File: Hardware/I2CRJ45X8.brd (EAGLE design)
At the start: 80 x 50 mm, 56 parts, among them IC1 MCP23017SO, IC2 MCP23017SO, J1 I2C-BREAKOUT, J2 INT2A, J3 M02X3-PIN, J4 M02X3-PIN, J5 RJ45-X8, J6 I2C-BREAKOUT, J7 INT1A

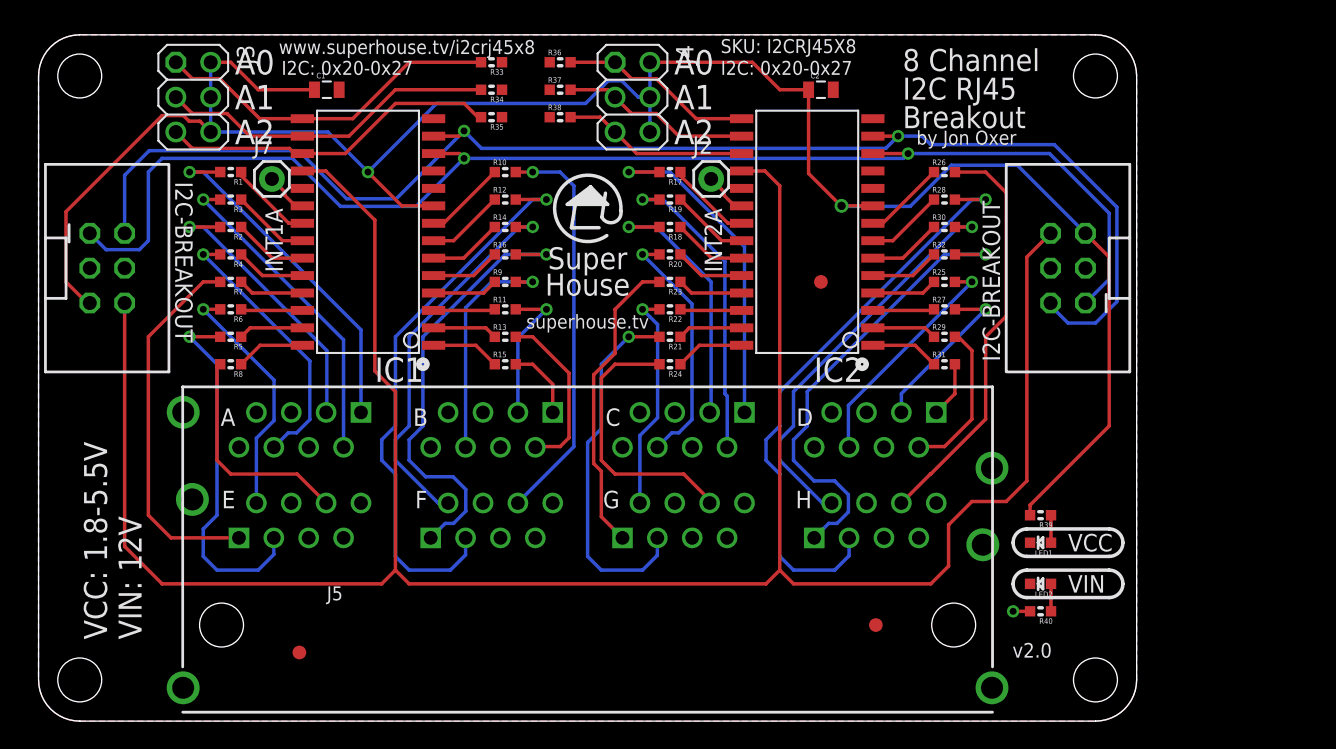
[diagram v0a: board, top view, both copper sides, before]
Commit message: Reduced width of PCB. Adjusted mounting hole locations. Improved GND connections. Changed position of power LEDs.
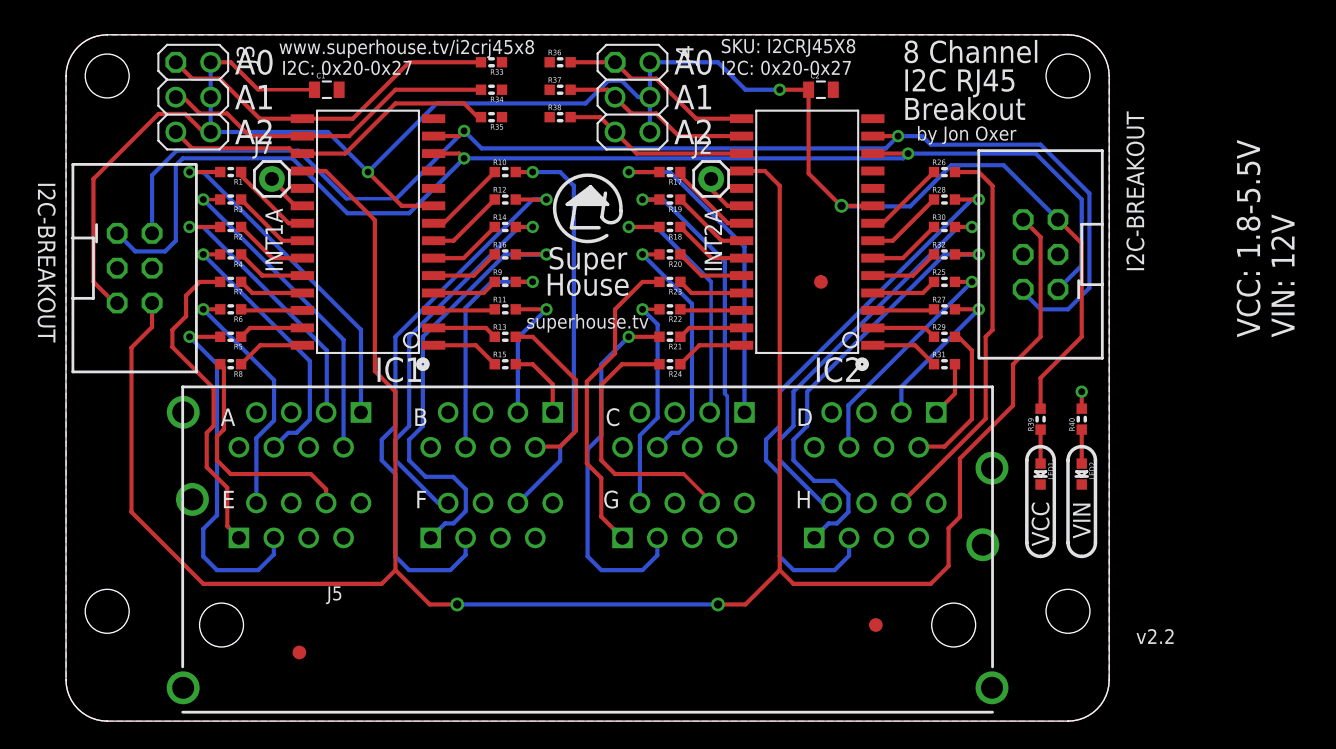
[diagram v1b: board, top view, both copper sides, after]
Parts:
- moved R40 14.3 mm to (76.0, 22.0), turned to 90 degrees
- moved LED2 8.54 mm to (76.0, 18.0), turned to 270 degrees
- moved R39 7.00 mm to (73.0, 22.0), turned to 90 degrees
- moved LED1 5.00 mm to (73.0, 18.0), turned to 270 degrees
- moved J1 2.24 mm to (73.0, 34.0)
- moved J6 2.00 mm to (7.00, 33.0)
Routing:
- net VCC: track 151.1 -> 140.3 mm, vias 2 -> 3
- net SDA: track 101.1 -> 96.7 mm
- net E1: track 27.2 -> 23.4 mm
- net SCL: track 97.5 -> 93.9 mm
- net H6: track 30.2 -> 29.0 mm
- net H3: track 43.1 -> 42.1 mm
- net H1: track 34.4 -> 33.4 mm
- net E6: track 16.3 -> 17.1 mm
- net D3: track 12.3 -> 11.6 mm
- net !RESET: track 174.0 -> 173.6 mm, vias 0 -> 2
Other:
- board size 80 x 50 mm -> 76 x 50 mm
- board text added: "(C)2019-2021 SuperHouse Automation Pty Ltd Released under the terms of the TAPR Open Hardware License: www.tapr.org/OHL"
- board text added: "v2.2"
- board text removed: "(C)2019-2020 SuperHouse Automation Pty Ltd Released under the terms of the TAPR Open Hardware License: www.tapr.org/OHL"
- board text removed: "v2.0"

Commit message: Silkscreen, clearances, and DRC for v2.2 release.
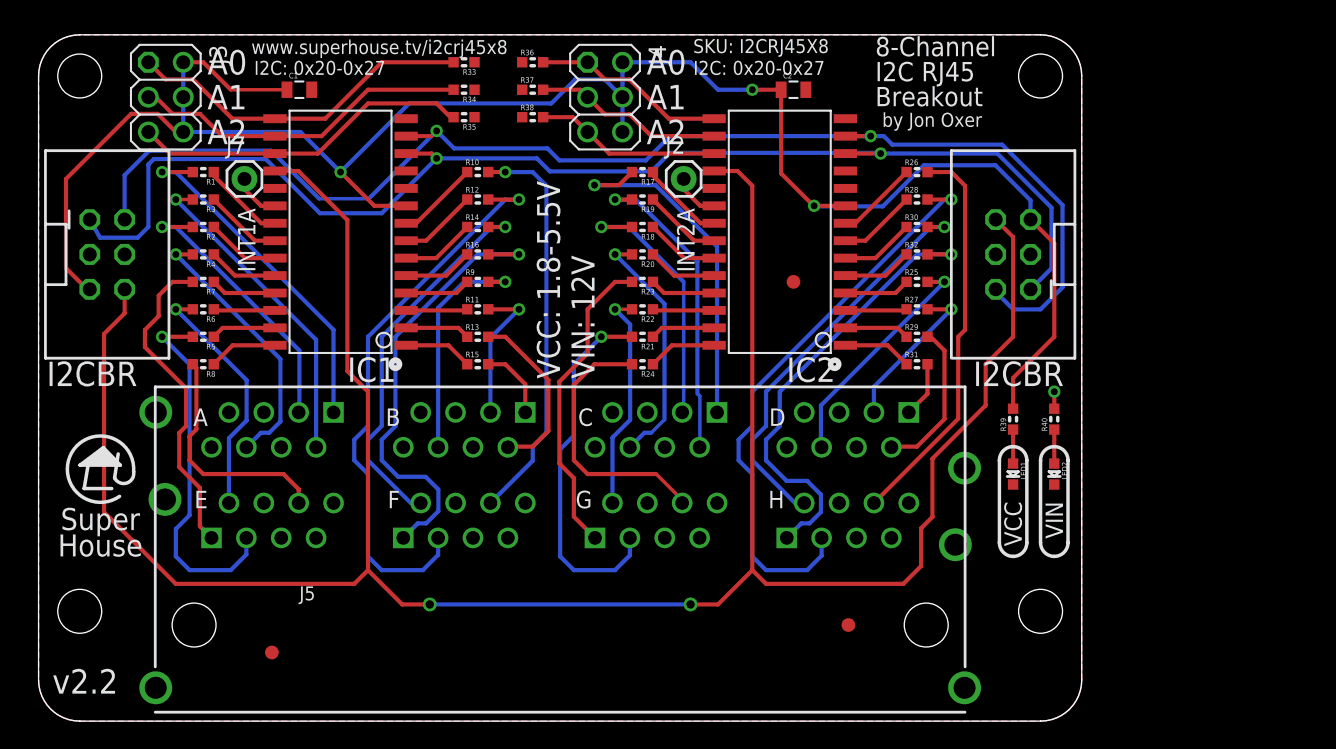
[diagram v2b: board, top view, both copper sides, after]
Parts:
- moved J6 2.24 mm to (5.00, 34.0)
- moved C1 2.00 mm to (19.0, 46.0)
- moved C2 2.00 mm to (55.0, 46.0)
- moved FID1 2.00 mm to (59.0, 7.00)
- moved FID2 2.00 mm to (17.0, 5.00)
- moved FID3 2.00 mm to (55.0, 32.0)
- moved IC1 2.00 mm to (22.0, 35.0)
- moved IC2 2.00 mm to (54.0, 35.0)
- moved J1 2.00 mm to (71.0, 34.0)
- moved J2 2.00 mm to (47.0, 39.5)
- moved J3 2.00 mm to (8.00, 48.0)
- moved J4 2.00 mm to (40.0, 48.0)
- moved J5 2.00 mm to (38.0, 7.00)
- moved J7 2.00 mm to (15.0, 39.5)
- moved LED1 2.00 mm to (71.0, 18.0)
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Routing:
- net C1: track 25.0 -> 26.0 mm
- net !RESET: track 173.6 -> 174.6 mm
- net SDA: track 96.7 -> 96.0 mm
- net SCL: track 93.9 -> 93.3 mm
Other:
- board text added: "8-Channel I2C RJ45 Breakout"
- board text added: "I2CBR"
- board text removed: "8 Channel I2C RJ45 Breakout"
- board text removed: "I2C-BREAKOUT"
- board text removed: "superhouse.tv"

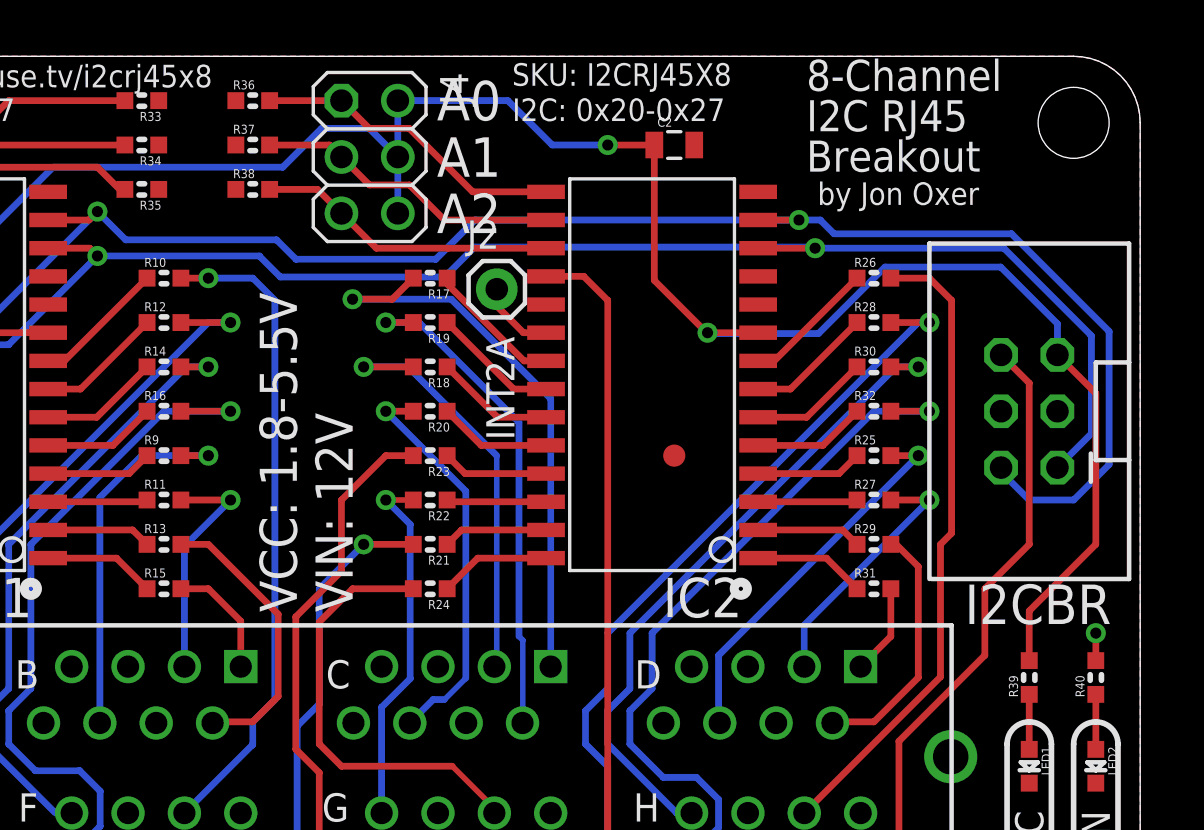
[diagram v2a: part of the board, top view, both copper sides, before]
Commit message: Added I2C pullups and silkscreen improvements.
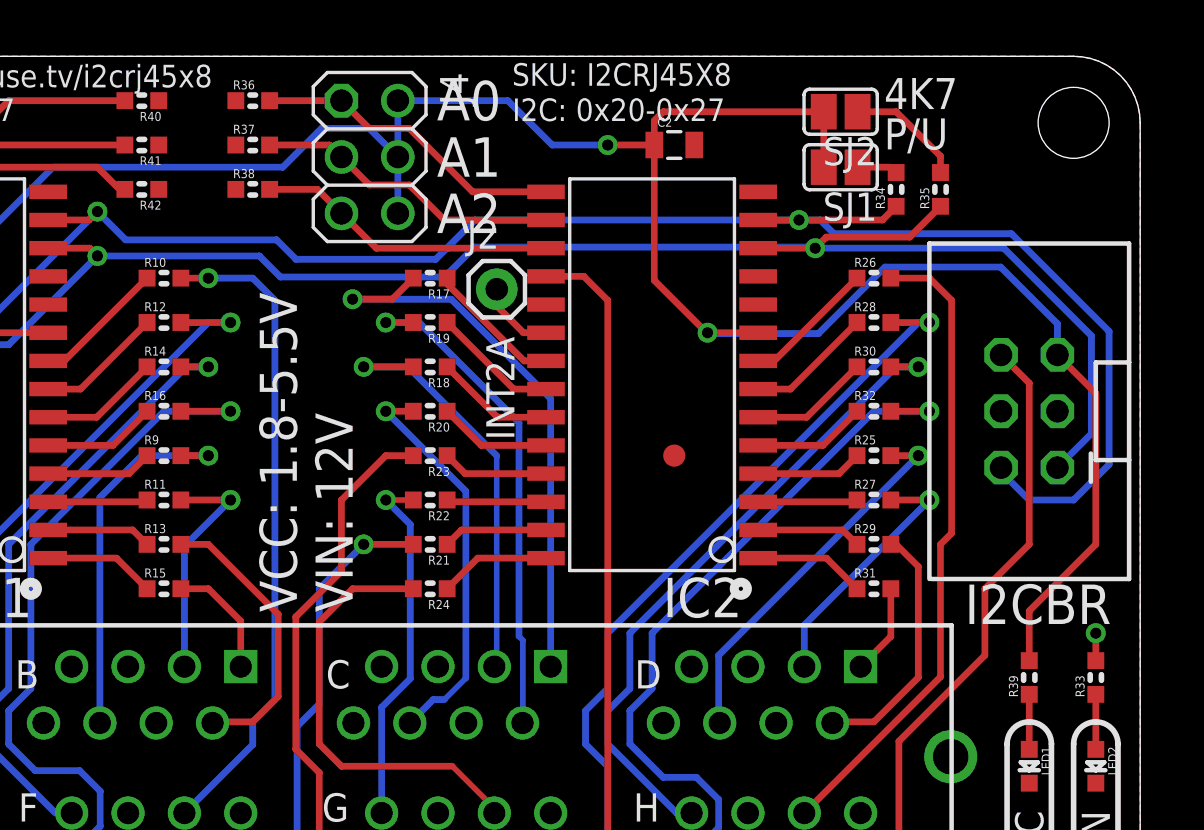
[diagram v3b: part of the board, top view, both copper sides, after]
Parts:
- added R41, R42: 10K, SuperHouse-DiscreteSemi:R0603
- added SJ1, SJ2: (no value), SuperHouse-Jumpers:SJ
- R33: value 10K -> 1K
- R34, R35: value 10K -> 4K7
- R40: value 1K -> 10K
- moved R33 50.2 mm to (74.0, 22.0), turned to 90 degrees
- moved R40 50.2 mm to (31.0, 48.0), turned to 180 degrees
- moved R35 36.0 mm to (67.0, 44.0), turned to 90 degrees
- moved R34 34.1 mm to (65.0, 44.0), turned to 90 degrees
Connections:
- new net N$11: R34.2, SJ1.1
- new net N$12: R35.2, SJ2.1
- net GND: now also R40.1, R41.1, R42.1; no longer R33.1, R34.1, R35.1
- net N$2: now also R42.2; no longer R35.2
- net N$3: now also R41.2; no longer R34.2
- net N$4: now also R40.2; no longer R33.2
- net N$8: now also R33.1; no longer R40.1
- net SCL: now also R35.1
- net SDA: now also R34.1
- net VCC: now also SJ1.2, SJ2.2
- net VIN: now also R33.2; no longer R40.2
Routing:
- net VCC: track 140.4 -> 151.8 mm
- net SCL: track 93.3 -> 99.7 mm
- net N$12: track 0.00 -> 5.30 mm
- net SDA: track 96.0 -> 100.6 mm
- net N$11: track 0.00 -> 1.84 mm
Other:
- board text added: "4K7 P/U"
- board text added: "www.superhouse.tv"
